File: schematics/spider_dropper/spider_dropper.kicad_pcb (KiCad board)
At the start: 2 copper layers, 80 x 20 mm, 10 parts, among them J1 JST_XH_3, J2 PJ-044AH, J3 JST_XH_2, Q1 IRLZ34N, SW1 ZX40E20C01

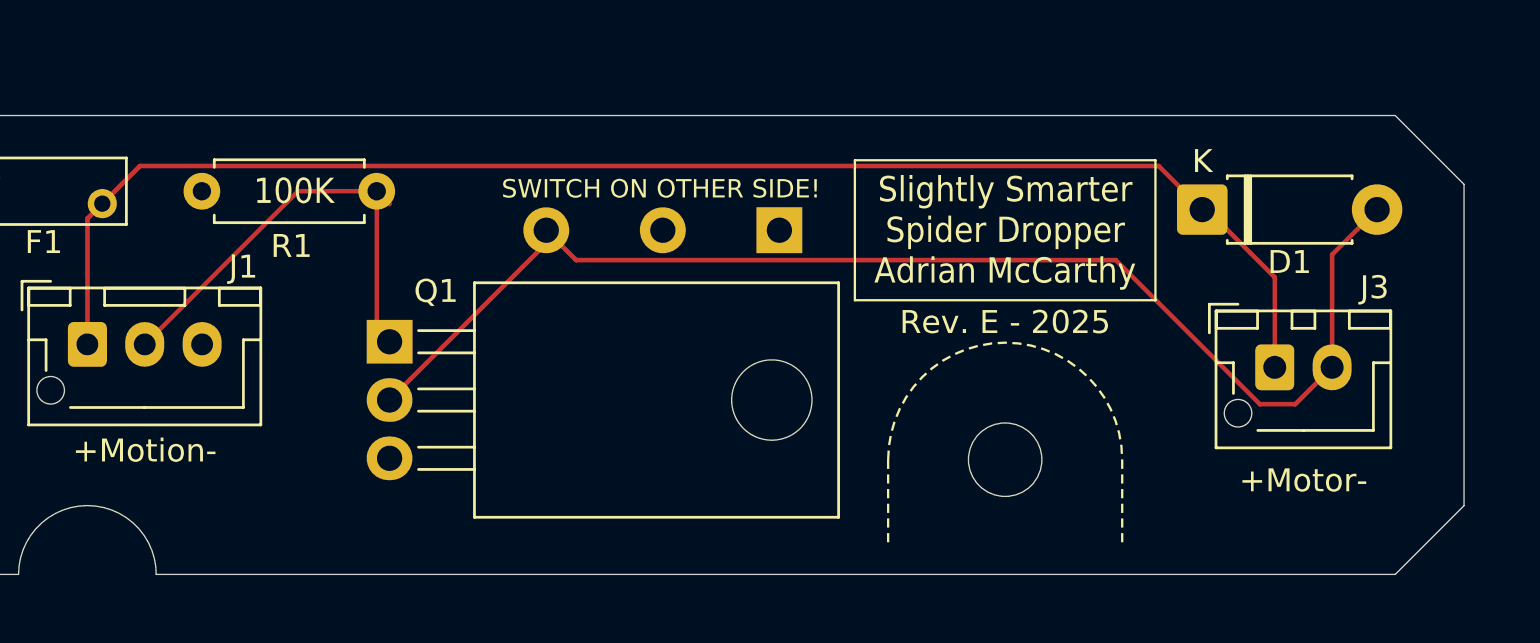
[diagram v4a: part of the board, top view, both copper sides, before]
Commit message: Switched to smaller, cheaper signal diode.
The 1N4001 was overkill for the motor flyback.  The 1N4148 is a common
signal diode that fits the space a little better.

Also nudged the connector for the motor controller to help my fat
fingers access it.
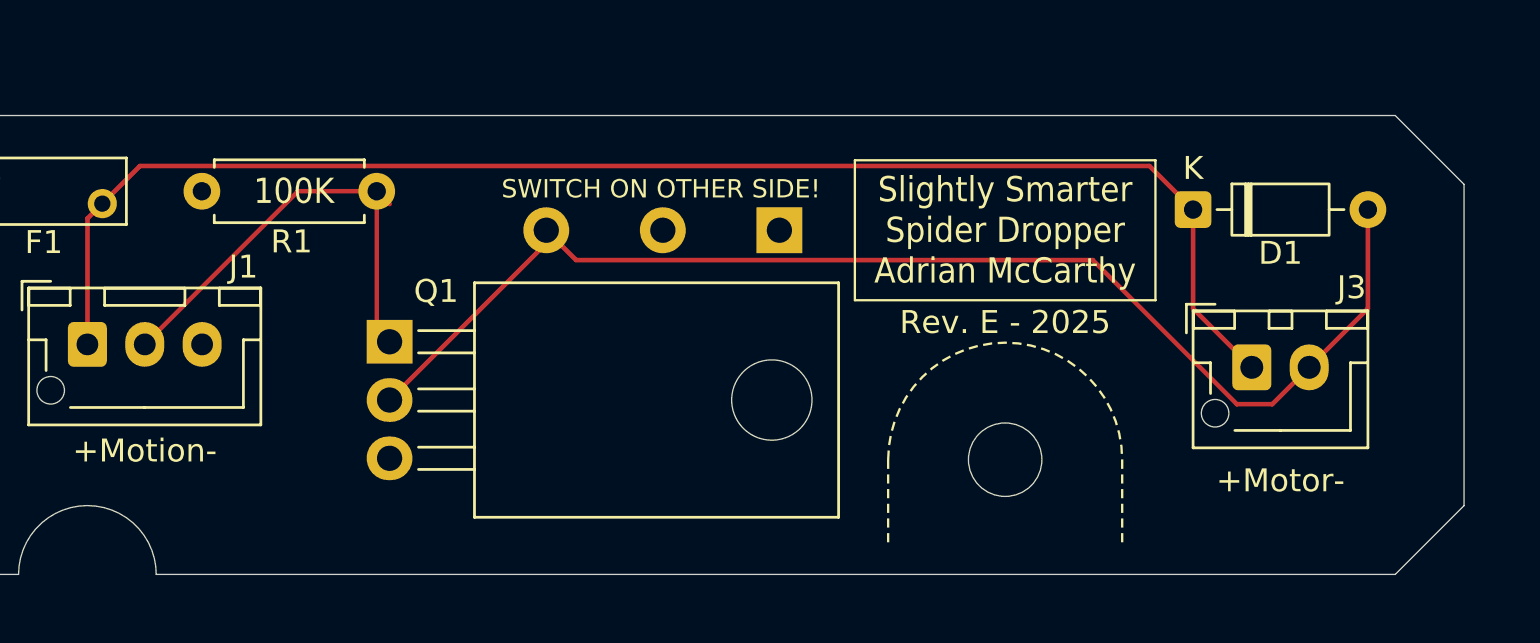
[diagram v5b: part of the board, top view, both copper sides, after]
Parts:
- D1: value 1N4001 -> 1N4148; footprint Diode_THT:D_DO-41_SOD81_P7.62mm_Horizontal -> Diode_THT:D_DO-35_SOD27_P7.62mm_Horizontal
- moved J3 1.00 mm to (180.7, 109.3)
- moved D1 0.40 mm to (178.1, 102.4)
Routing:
- net /MOTOR+: track 64.2 -> 63.3 mm
- net /MOTOR-: track 56.0 -> 55.2 mm
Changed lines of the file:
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@@
 	(title_block
 		(title "Slightly Smarter Simple Spider Dropper")
-		(date "2025-09-21")
+		(date "2025-09-27")
 		(rev "E")
 		(company "Adrian McCarthy")
@@
 		(comment 7 "nudged diode away from corner")
 		(comment 8 "added arrow on b. silkscreen")
+		(comment 9 "changed D1 and nudged J3 even more")
 	)
 	(layers
@@
 	(net 6 "/MOTION")
 	(net 7 "unconnected-(J2-Pad3)")
-	(footprint "Diode_THT:D_DO-41_SOD81_P7.62mm_Horizontal"
+	(footprint "Diode_THT:D_DO-35_SOD27_P7.62mm_Horizontal"
 		(layer "F.Cu")
-		(at 178.49 102.4)
-		(descr "Diode, DO-41_SOD81 series, Axial, Horizontal, pin pitch=7.62mm, length*diameter=5.2*2.7mm^2, https://www.diodes.com/assets/Package-Files/DO-41-Plastic.pdf")
-		(tags "Diode DO-41_SOD81 series Axial Horizontal pin pitch 7.62mm  length 5.2mm diameter 2.7mm")
+		(at 178.09 102.4)
+		(descr "Diode, DO-35_SOD27 series, Axial, Horizontal, pin pitch=7.62mm, length*diameter=4*2mm^2, http://www.diodes.com/_files/packages/DO-35.pdf")
+		(tags "Diode DO-35_SOD27 series Axial Horizontal pin pitch 7.62mm  length 4mm diameter 2mm")
 		(property "Reference" "D1"
-			(at 3.81 2.3 0)
+			(at 3.81 1.9 0)
 			(layer "F.SilkS")
 			(effects
@@
 			)
 		)
-		(property "Value" "1N4001"
-			(at 3.81 2.47 0)
+		(property "Value" "1N4148"
+			(at 3.81 2.12 0)
 			(layer "F.Fab")
 			(effects
@@
 		(attr through_hole)
 		(fp_line
-			(start 1.09 -1.47)
-			(end 6.53 -1.47)
+			(start 1.04 0)
+			(end 1.69 0)
 			(stroke
 				(width 0.12)
@@
 		)
 		(fp_line
-			(start 1.09 -1.34)
-			(end 1.09 -1.47)
+			(start 2.29 -1.12)
+			(end 2.29 1.12)
 			(stroke
 				(width 0.12)
@@
 		)
 		(fp_line
-			(start 1.09 1.34)
-			(end 1.09 1.47)
+			(start 2.41 -1.12)
+			(end 2.41 1.12)
 			(stroke
 				(width 0.12)
@@
 		)
 		(fp_line
-			(start 1.09 1.47)
-			(end 6.53 1.47)
+			(start 2.53 -1.12)
+			(end 2.53 1.12)
 			(stroke
 				(width 0.12)
@@
 		)
 		(fp_line
-			(start 1.87 -1.47)
-			(end 1.87 1.47)
+			(start 6.58 0)
+			(end 5.93 0)
 			(stroke
 				(width 0.12)
@@
 			(layer "F.SilkS")
 		)
-		(fp_line
-			(start 1.99 -1.47)
-			(end 1.99 1.47)
-			(stroke
-				(width 0.12)
-				(type solid)
-			)
-			(layer "F.SilkS")
-		)
-		(fp_line
-			(start 2.11 -1.47)
-			(end 2.11 1.47)
-			(stroke
-				(width 0.12)
-				(type solid)
-			)
-			(layer "F.SilkS")
-		)
-		(fp_line
-			(start 6.53 -1.47)
-			(end 6.53 -1.34)
-			(stroke
-				(width 0.12)
-				(type solid)
-			)
-			(layer "F.SilkS")
-		)
-		(fp_line
-			(start 6.53 1.47)
-			(end 6.53 1.34)
+		(fp_rect
+			(start 1.69 -1.12)
+			(end 5.93 1.12)
 			(stroke
 				(width 0.12)
 				(type solid)
 			)
+			(fill no)
 			(layer "F.SilkS")
 		)
 		(fp_rect
-			(start -1.35 -1.6)
-			(end 8.97 1.6)
+			(start -1.05 -1.25)
+			(end 8.67 1.25)
 			(stroke
 				(width 0.05)
@@
 		(fp_line
 			(start 0 0)
-			(end 1.21 0)
+			(end 1.81 0)
 			(stroke
 				(width 0.1)
@@
 		)
 		(fp_line
-			(start 1.89 -1.35)
-			(end 1.89 1.35)
+			(start 2.31 -1)
+			(end 2.31 1)
 			(stroke
 				(width 0.1)
@@
 		)
 		(fp_line
-			(start 1.99 -1.35)
-			(end 1.99 1.35)
+			(start 2.41 -1)
+			(end 2.41 1)
 			(stroke
 				(width 0.1)
@@
 		)
 		(fp_line
-			(start 2.09 -1.35)
-			(end 2.09 1.35)
+			(start 2.51 -1)
+			(end 2.51 1)
 			(stroke
 				(width 0.1)
@@
 		(fp_line
 			(start 7.62 0)
-			(end 6.41 0)
+			(end 5.81 0)
 			(stroke
 				(width 0.1)
@@
 		)
 		(fp_rect
-			(start 1.21 -1.35)
-			(end 6.41 1.35)
+			(start 1.81 -1)
+			(end 5.81 1)
 			(stroke
 				(width 0.1)
@@
 		)
 		(fp_text user "K"
-			(at 0 -2.1 0)
+			(at 0 -1.8 0)
 			(layer "F.SilkS")
 			(effects
@@
 		)
 		(fp_text user "${REFERENCE}"
-			(at 4.2 0 0)
+			(at 4.11 0 0)
 			(layer "F.Fab")
 			(effects
 				(font
-					(size 1 1)
-					(thickness 0.15)
+					(size 0.8 0.8)
+					(thickness 0.12)
 				)
 			)
 		)
 		(fp_text user "K"
-			(at 0 -2.1 0)
+			(at 0 -1.8 0)
 			(layer "F.Fab")
 			(effects
@@
 		(pad "1" thru_hole roundrect
 			(at 0 0)
-			(size 2.2 2.2)
-			(drill 1.1)
+			(size 1.6 1.6)
+			(drill 0.8)
 			(layers "*.Cu" "*.Mask")
 			(remove_unused_layers no)
-			(roundrect_rratio 0.113636)
+			(roundrect_rratio 0.15625)
 			(net 4 "/MOTOR+")
 			(pinfunction "K")
@@
 		(pad "2" thru_hole circle
 			(at 7.62 0)
-			(size 2.2 2.2)
-			(drill 1.1)
+			(size 1.6 1.6)
+			(drill 0.8)
 			(layers "*.Cu" "*.Mask")
 			(remove_unused_layers no)
@@
 		)
 		(embedded_fonts no)
-		(model "${KICAD9_3DMODEL_DIR}/Diode_THT.3dshapes/D_DO-41_SOD81_P7.62mm_Horizontal.step"
+		(model "${KICAD9_3DMODEL_DIR}/Diode_THT.3dshapes/D_DO-35_SOD27_P7.62mm_Horizontal.step"
 			(offset
 				(xyz 0 0 0)
@@
 		(tags "Resistor Axial_DIN0207 series Axial Horizontal pin pitch 7.62mm 0.25W = 1/4W length 6.3mm diameter 2.5mm")
 		(property "Reference" "R1"
-			(at 3.71 -2.4 0)
+			(at 3.71 -2.2 0)
 			(layer "F.SilkS")
 			(effects
@@
 	(footprint "Connector_JST:JST_XH_B2B-XH-AM_1x02_P2.50mm_Vertical"
 		(layer "F.Cu")
-		(at 181.65 109.275)
+		(at 180.65 109.275)
 		(descr "JST XH series connector, B2B-XH-AM, with boss (http://www.jst-mfg.com/product/pdf/eng/eXH.pdf), generated with kicad-footprint-generator")
 		(tags "connector JST XH vertical boss")
@@
 		(tags "mountinghole M3")
 		(property "Reference" "H1"
-			(at 6.3 -1.4 180)
+			(at 4.7 -0.5 180)
 			(layer "B.SilkS")
 			(effects
@@
 	)
 	(gr_text "+Motor-"
-		(at 182.9 114.8 0)
+		(at 181.9 114.8 0)
 		(layer "F.SilkS")
 		(effects
@@
 	)
 	(gr_text "M3"
-		(at 177.3 113.3 0)
+		(at 175.7 114.2 0)
 		(layer "B.SilkS")
 		(effects
@@
 	)
 	(segment
-		(start 132.191 100.499)
-		(end 176.589 100.499)
-		(width 0.2)
-		(layer "F.Cu")
-		(net 4)
-	)
-	(segment
-		(start 181.65 105.35)
-		(end 181.65 109.275)
-		(width 0.2)
-		(layer "F.Cu")
-		(net 4)
-	)
-	(segment
-		(start 181.65 105.35)
-		(end 178.7 102.4)
+		(start 178.09 106.715)
+		(end 180.65 109.275)
 		(width 0.2)
 		(layer "F.Cu")
@@
 	)
 	(segment
-		(start 178.7 102.4)
-		(end 178.49 102.4)
+		(start 176.189 100.499)
+		(end 178.09 102.4)
 		(width 0.2)
 		(layer "F.Cu")
@@
 	)
 	(segment
-		(start 178.89 102.5)
-		(end 178.89 102.59)
+		(start 129.9 108.275)
+		(end 129.9 102.79)
 		(width 0.2)
 		(layer "F.Cu")
@@
 	)
 	(segment
-		(start 129.9 108.275)
-		(end 129.9 102.79)
+		(start 129.9 102.79)
+		(end 130.55 102.14)
 		(width 0.2)
 		(layer "F.Cu")
@@
 	)
 	(segment
-		(start 129.9 102.79)
-		(end 130.55 102.14)
+		(start 132.191 100.499)
+		(end 176.189 100.499)
 		(width 0.2)
 		(layer "F.Cu")
@@
 	)
 	(segment
-		(start 176.589 100.499)
-		(end 178.49 102.4)
+		(start 178.09 102.4)
+		(end 178.09 106.715)
 		(width 0.2)
 		(layer "F.Cu")
@@
 	)
 	(segment
-		(start 151.201 104.601)
-		(end 149.9 103.3)
+		(start 149.9 103.87)
+		(end 143.07 110.7)
 		(width 0.2)
 		(layer "F.Cu")
@@
 	)
 	(segment
-		(start 182.543917 110.881083)
-		(end 181.001 110.881083)
+		(start 183.15 109.275)
+		(end 181.543917 110.881083)
 		(width 0.2)
 		(layer "F.Cu")
@@
 	)
 	(segment
-		(start 181.001 110.881083)
-		(end 174.720917 104.601)
+		(start 185.71 102.4)
+		(end 185.71 106.715)
 		(width 0.2)
 		(layer "F.Cu")
@@
 	)
 	(segment
-		(start 143.07 110.7)
-		(end 149.9 103.87)
+		(start 180.001 110.881083)
+		(end 173.720917 104.601)
 		(width 0.2)
 		(layer "F.Cu")
@@
 	)
 	(segment
-		(start 174.720917 104.601)
-		(end 151.201 104.601)
+		(start 185.71 106.715)
+		(end 183.15 109.275)
 		(width 0.2)
 		(layer "F.Cu")
@@
 	)
 	(segment
-		(start 184.15 104.36)
-		(end 186.11 102.4)
+		(start 149.9 103.3)
+		(end 149.9 103.87)
 		(width 0.2)
 		(layer "F.Cu")
@@
 	)
 	(segment
-		(start 184.15 109.275)
-		(end 184.15 104.36)
+		(start 173.720917 104.601)
+		(end 151.201 104.601)
 		(width 0.2)
 		(layer "F.Cu")
@@
 	)
 	(segment
-		(start 184.15 109.275)
-		(end 182.543917 110.881083)
+		(start 151.201 104.601)
+		(end 149.9 103.3)
 		(width 0.2)
 		(layer "F.Cu")
@@
 	)
 	(segment
-		(start 149.9 103.87)
-		(end 149.9 103.3)
+		(start 181.543917 110.881083)
+		(end 180.001 110.881083)
 		(width 0.2)
 		(layer "F.Cu")

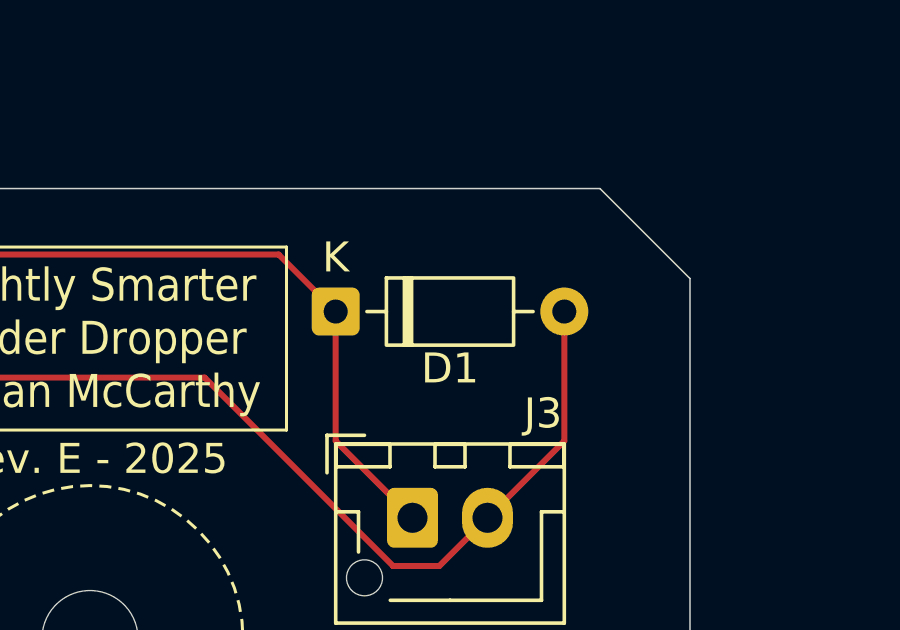
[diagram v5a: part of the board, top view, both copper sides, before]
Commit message: Reverted change to the diode.  Back to 1N4001.
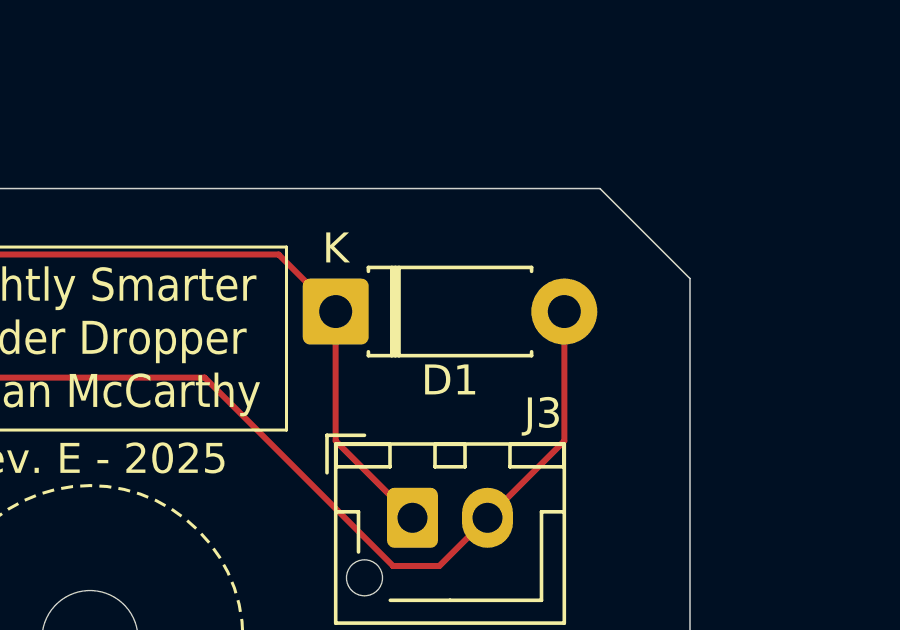
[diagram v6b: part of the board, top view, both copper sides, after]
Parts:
- D1: value 1N4148 -> 1N4001; footprint Diode_THT:D_DO-35_SOD27_P7.62mm_Horizontal -> Diode_THT:D_DO-41_SOD81_P7.62mm_Horizontal
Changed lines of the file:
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@@
 	(title_block
 		(title "Slightly Smarter Simple Spider Dropper")
-		(date "2025-09-27")
+		(date "2025-10-14")
 		(rev "E")
 		(company "Adrian McCarthy")
@@
 		(comment 7 "nudged diode away from corner")
 		(comment 8 "added arrow on b. silkscreen")
-		(comment 9 "changed D1 and nudged J3 even more")
+		(comment 9 "nudged J3 even more")
 	)
 	(layers
@@
 	(net 6 "/MOTION")
 	(net 7 "unconnected-(J2-Pad3)")
-	(footprint "Diode_THT:D_DO-35_SOD27_P7.62mm_Horizontal"
+	(footprint "Diode_THT:D_DO-41_SOD81_P7.62mm_Horizontal"
 		(layer "F.Cu")
 		(at 178.09 102.4)
-		(descr "Diode, DO-35_SOD27 series, Axial, Horizontal, pin pitch=7.62mm, length*diameter=4*2mm^2, http://www.diodes.com/_files/packages/DO-35.pdf")
-		(tags "Diode DO-35_SOD27 series Axial Horizontal pin pitch 7.62mm  length 4mm diameter 2mm")
+		(descr "Diode, DO-41_SOD81 series, Axial, Horizontal, pin pitch=7.62mm, length*diameter=5.2*2.7mm^2, https://www.diodes.com/assets/Package-Files/DO-41-Plastic.pdf")
+		(tags "Diode DO-41_SOD81 series Axial Horizontal pin pitch 7.62mm  length 5.2mm diameter 2.7mm")
 		(property "Reference" "D1"
-			(at 3.81 1.9 0)
-			(layer "F.SilkS")
-			(effects
-				(font
-					(size 1 1)
-					(thickness 0.15)
-				)
-			)
-		)
-		(property "Value" "1N4148"
-			(at 3.81 2.12 0)
+			(at 3.81 2.3 0)
+			(layer "F.SilkS")
+			(effects
+				(font
+					(size 1 1)
+					(thickness 0.15)
+				)
+			)
+		)
+		(property "Value" "1N4001"
+			(at 3.81 2.47 0)
 			(layer "F.Fab")
 			(effects
@@
 		(attr through_hole)
 		(fp_line
-			(start 1.04 0)
-			(end 1.69 0)
-			(stroke
-				(width 0.12)
-				(type solid)
-			)
-			(layer "F.SilkS")
-		)
-		(fp_line
-			(start 2.29 -1.12)
-			(end 2.29 1.12)
-			(stroke
-				(width 0.12)
-				(type solid)
-			)
-			(layer "F.SilkS")
-		)
-		(fp_line
-			(start 2.41 -1.12)
-			(end 2.41 1.12)
-			(stroke
-				(width 0.12)
-				(type solid)
-			)
-			(layer "F.SilkS")
-		)
-		(fp_line
-			(start 2.53 -1.12)
-			(end 2.53 1.12)
-			(stroke
-				(width 0.12)
-				(type solid)
-			)
-			(layer "F.SilkS")
-		)
-		(fp_line
-			(start 6.58 0)
-			(end 5.93 0)
+			(start 1.09 -1.47)
+			(end 6.53 -1.47)
+			(stroke
+				(width 0.12)
+				(type solid)
+			)
+			(layer "F.SilkS")
+		)
+		(fp_line
+			(start 1.09 -1.34)
+			(end 1.09 -1.47)
+			(stroke
+				(width 0.12)
+				(type solid)
+			)
+			(layer "F.SilkS")
+		)
+		(fp_line
+			(start 1.09 1.34)
+			(end 1.09 1.47)
+			(stroke
+				(width 0.12)
+				(type solid)
+			)
+			(layer "F.SilkS")
+		)
+		(fp_line
+			(start 1.09 1.47)
+			(end 6.53 1.47)
+			(stroke
+				(width 0.12)
+				(type solid)
+			)
+			(layer "F.SilkS")
+		)
+		(fp_line
+			(start 1.87 -1.47)
+			(end 1.87 1.47)
+			(stroke
+				(width 0.12)
+				(type solid)
+			)
+			(layer "F.SilkS")
+		)
+		(fp_line
+			(start 1.99 -1.47)
+			(end 1.99 1.47)
+			(stroke
+				(width 0.12)
+				(type solid)
+			)
+			(layer "F.SilkS")
+		)
+		(fp_line
+			(start 2.11 -1.47)
+			(end 2.11 1.47)
+			(stroke
+				(width 0.12)
+				(type solid)
+			)
+			(layer "F.SilkS")
+		)
+		(fp_line
+			(start 6.53 -1.47)
+			(end 6.53 -1.34)
+			(stroke
+				(width 0.12)
+				(type solid)
+			)
+			(layer "F.SilkS")
+		)
+		(fp_line
+			(start 6.53 1.47)
+			(end 6.53 1.34)
 			(stroke
 				(width 0.12)
@@
 		)
 		(fp_rect
-			(start 1.69 -1.12)
-			(end 5.93 1.12)
-			(stroke
-				(width 0.12)
-				(type solid)
-			)
-			(fill no)
-			(layer "F.SilkS")
-		)
-		(fp_rect
-			(start -1.05 -1.25)
-			(end 8.67 1.25)
+			(start -1.35 -1.6)
+			(end 8.97 1.6)
 			(stroke
 				(width 0.05)
@@
 		(fp_line
 			(start 0 0)
-			(end 1.81 0)
-			(stroke
-				(width 0.1)
-				(type solid)
-			)
-			(layer "F.Fab")
-		)
-		(fp_line
-			(start 2.31 -1)
-			(end 2.31 1)
-			(stroke
-				(width 0.1)
-				(type solid)
-			)
-			(layer "F.Fab")
-		)
-		(fp_line
-			(start 2.41 -1)
-			(end 2.41 1)
-			(stroke
-				(width 0.1)
-				(type solid)
-			)
-			(layer "F.Fab")
-		)
-		(fp_line
-			(start 2.51 -1)
-			(end 2.51 1)
+			(end 1.21 0)
+			(stroke
+				(width 0.1)
+				(type solid)
+			)
+			(layer "F.Fab")
+		)
+		(fp_line
+			(start 1.89 -1.35)
+			(end 1.89 1.35)
+			(stroke
+				(width 0.1)
+				(type solid)
+			)
+			(layer "F.Fab")
+		)
+		(fp_line
+			(start 1.99 -1.35)
+			(end 1.99 1.35)
+			(stroke
+				(width 0.1)
+				(type solid)
+			)
+			(layer "F.Fab")
+		)
+		(fp_line
+			(start 2.09 -1.35)
+			(end 2.09 1.35)
 			(stroke
 				(width 0.1)
@@
 		(fp_line
 			(start 7.62 0)
-			(end 5.81 0)
+			(end 6.41 0)
 			(stroke
 				(width 0.1)
@@
 		)
 		(fp_rect
-			(start 1.81 -1)
-			(end 5.81 1)
+			(start 1.21 -1.35)
+			(end 6.41 1.35)
 			(stroke
 				(width 0.1)
@@
 		)
 		(fp_text user "K"
-			(at 0 -1.8 0)
+			(at 0 -2.1 0)
 			(layer "F.SilkS")
 			(effects
@@
 		)
 		(fp_text user "${REFERENCE}"
-			(at 4.11 0 0)
-			(layer "F.Fab")
-			(effects
-				(font
-					(size 0.8 0.8)
-					(thickness 0.12)
+			(at 4.2 0 0)
+			(layer "F.Fab")
+			(effects
+				(font
+					(size 1 1)
+					(thickness 0.15)
 				)
 			)
 		)
 		(fp_text user "K"
-			(at 0 -1.8 0)
+			(at 0 -2.1 0)
 			(layer "F.Fab")
 			(effects
@@
 		(pad "1" thru_hole roundrect
 			(at 0 0)
-			(size 1.6 1.6)
-			(drill 0.8)
+			(size 2.2 2.2)
+			(drill 1.1)
 			(layers "*.Cu" "*.Mask")
 			(remove_unused_layers no)
-			(roundrect_rratio 0.15625)
+			(roundrect_rratio 0.113636)
 			(net 4 "/MOTOR+")
 			(pinfunction "K")
@@
 		(pad "2" thru_hole circle
 			(at 7.62 0)
-			(size 1.6 1.6)
-			(drill 0.8)
+			(size 2.2 2.2)
+			(drill 1.1)
 			(layers "*.Cu" "*.Mask")
 			(remove_unused_layers no)
@@
 		)
 		(embedded_fonts no)
-		(model "${KICAD9_3DMODEL_DIR}/Diode_THT.3dshapes/D_DO-35_SOD27_P7.62mm_Horizontal.step"
+		(model "${KICAD9_3DMODEL_DIR}/Diode_THT.3dshapes/D_DO-41_SOD81_P7.62mm_Horizontal.step"
 			(offset
 				(xyz 0 0 0)
